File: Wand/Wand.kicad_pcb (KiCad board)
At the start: 4 copper layers, 50 x 7 mm, 28 parts, among them P1 ISP, P2 KLB4, P3 BASE, U1 ATMEGA328-MMH, U2 OPA336, U3 MPU-6050

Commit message: Production files
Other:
- rule trace_min: 0.2 -> 0.13
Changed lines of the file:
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@@
     (zone_clearance 0.1)
     (zone_45_only no)
-    (trace_min 0.2)
+    (trace_min 0.13)
     (segment_width 0.2)
     (edge_width 0.15)

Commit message: Synced with schematic
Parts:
- R10: value 56K -> 10K
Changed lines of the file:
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@@
     (links 66)
     (no_connects 0)
-    (area 83.564287 99.6375 161.835715 132.377185)
+    (area 96.924999 108.424999 147.075001 115.575001)
     (thickness 1.6)
     (drawings 33)
@@
       (effects (font (size 0.5 0.5) (thickness 0.125)))
     )
-    (fp_text value 56K (at 0 1.8 270) (layer F.Fab)
+    (fp_text value 10K (at 0 1.8 270) (layer F.Fab)
       (effects (font (size 1 1) (thickness 0.15)))
     )

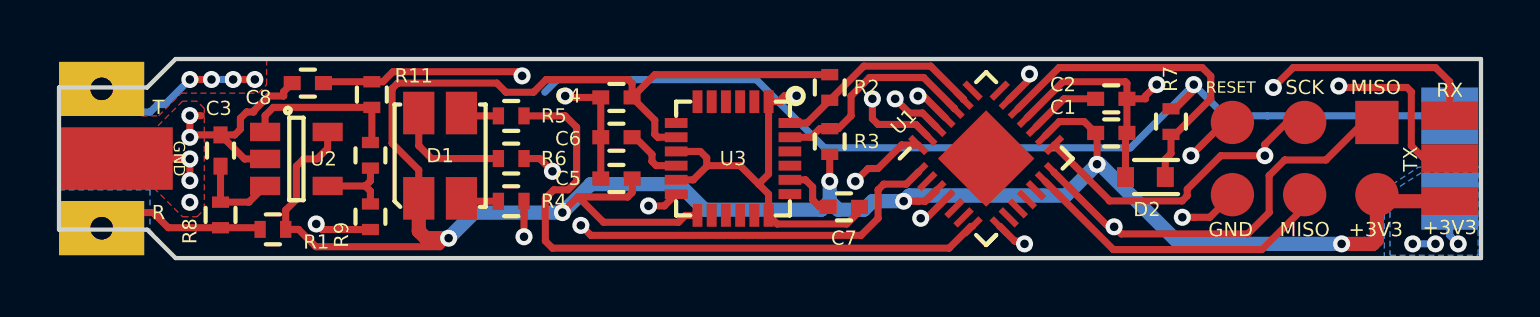
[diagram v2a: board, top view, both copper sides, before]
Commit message: Updated as per recommendations from PCB Way (0.25 mm gap between edge and traces.
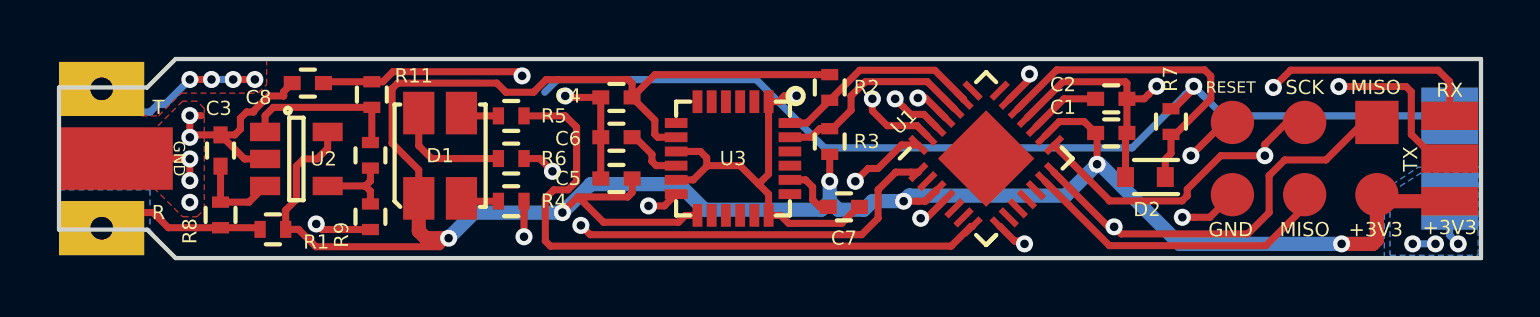
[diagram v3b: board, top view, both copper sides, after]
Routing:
- net /RESET: track 20.8 -> 20.1 mm
- net /TX: track 27.1 -> 26.4 mm
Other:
- board text added: "T/HEAT: Half hole R/SENS: Half hole"
